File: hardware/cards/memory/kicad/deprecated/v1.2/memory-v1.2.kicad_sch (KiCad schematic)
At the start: 0 parts

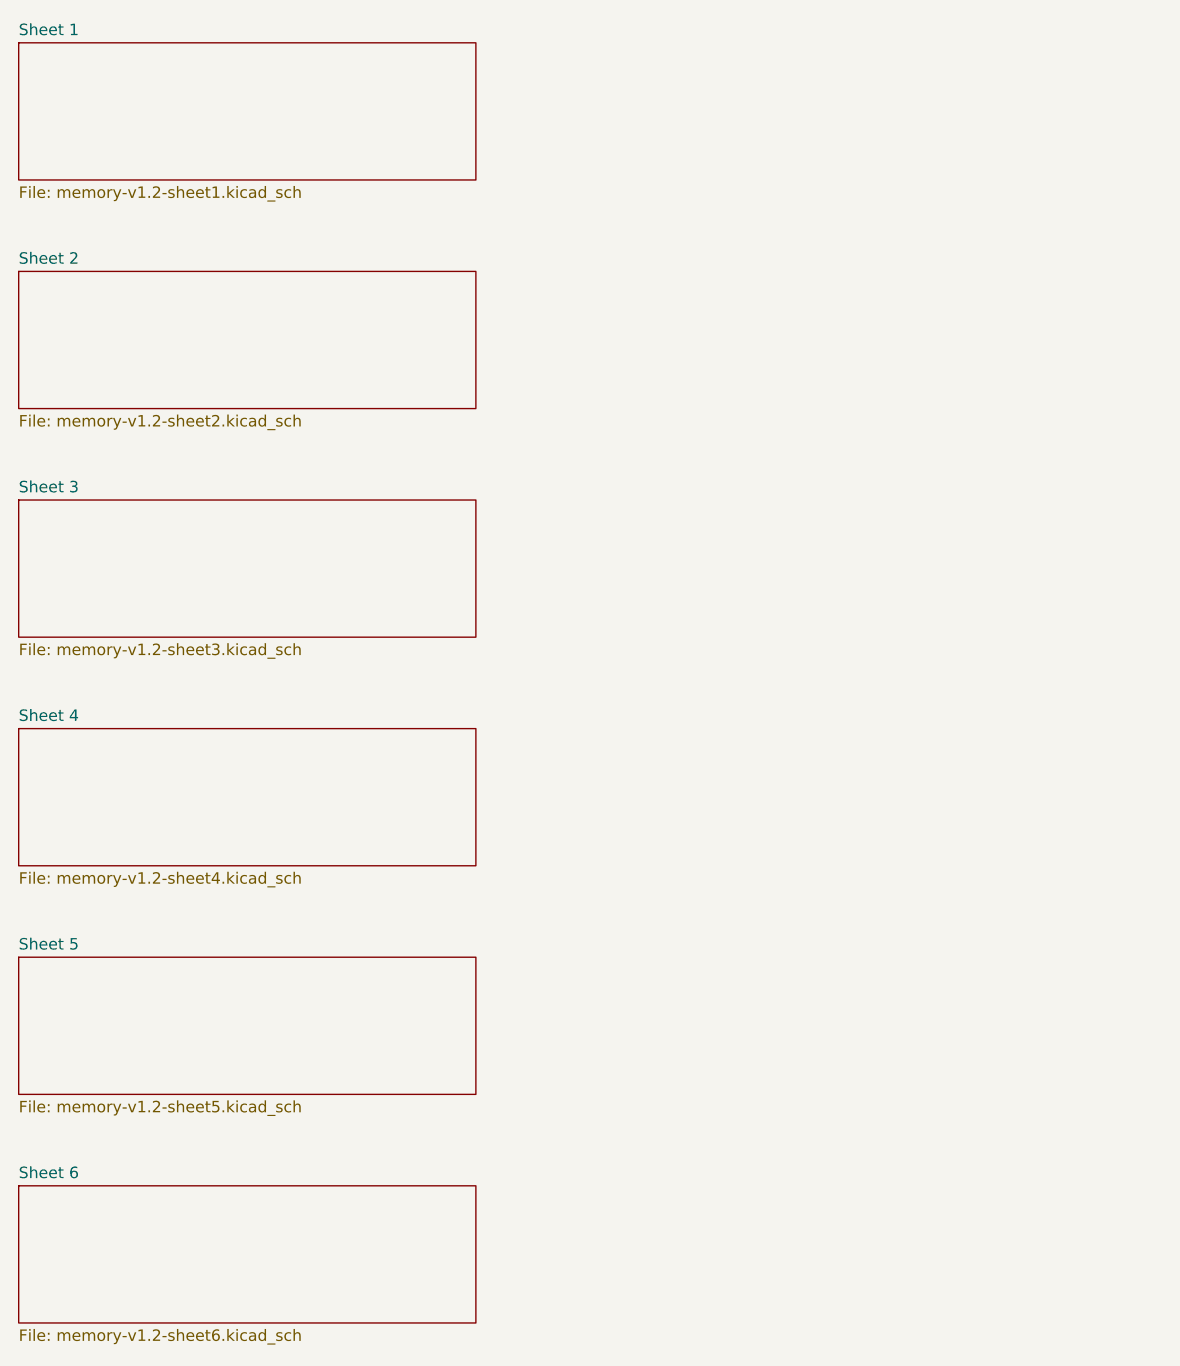
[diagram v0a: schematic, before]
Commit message: fix(kicad): readable converted schematics - overlaps 42,847 -> 3,147, nothing off the frame; CF sheet 0 overlaps
- tools/kicad/sch_overlaps.py: calibrated readability check (text/text, text/body, text/line, off frame/title block)
- eagle_sch_to_kicad.py: fields placed from Eagle's smashed attributes or the symbol's >NAME/>VALUE with Eagle's align,
  size and ratio, readable angles; fields Eagle never shows hidden (FABC96R shows only its pin name); pin numbers hidden
  where every Eagle pin hides them; Eagle-hidden layers dropped (the stray SpiceOrder text); labels on their own wires,
  converter labels only where KiCad needs them; rotate-then-mirror fixed for MR90/MR270 in pin_world/no-connects;
  each sheet on the smallest page that holds it, centred clear of the title block
- finish_board.py: stable footprint-library choice (DRC counts no longer vary run to run)
- all 37 projects regenerated: netlist proofs unchanged (34 MATCH, 2 schematic-only, video Fusion export MISMATCH as
  before); DRC same or better; ERC up (loose wire ends onto graphic buses no longer hidden by labels; explained per README)
- CF card: gate names off the gate bodies, U3 clear of its title, 5.08 mm connector pins; rebuilt: DRC 0/0, proof MATCH
- schematic PDFs regenerated (tools/sch_to_pdf.py, 37/37)

Co-Authored-By: Claude Opus 5.5 <noreply@anthropic.com>
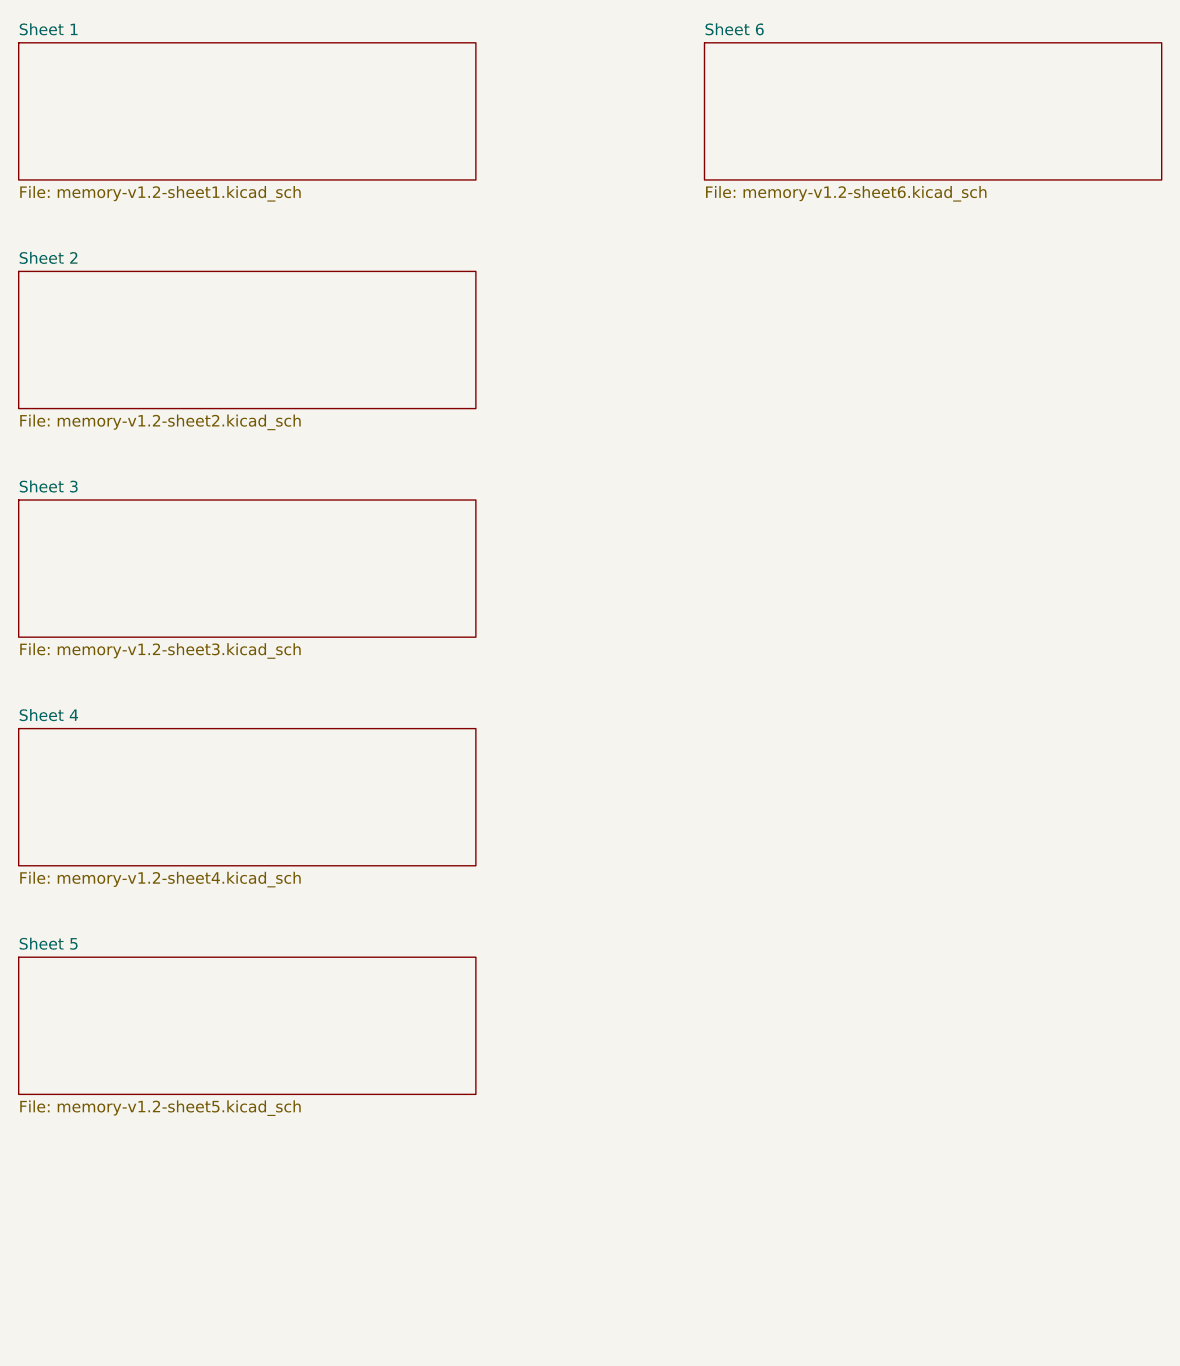
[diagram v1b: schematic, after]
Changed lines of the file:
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@@
 		(instances (project "memory-v1.2" (path "/af66b66e-c3aa-f1a5-6d3e-e2820af0deba" (page "6"))))
 	)
-	(sheet (at 25.4 152.4) (size 50.8 15.24) (exclude_from_sim no) (in_bom yes) (on_board yes) (dnp no) (fields_autoplaced yes)
+	(sheet (at 101.6 25.4) (size 50.8 15.24) (exclude_from_sim no) (in_bom yes) (on_board yes) (dnp no) (fields_autoplaced yes)
 		(stroke (width 0.1524) (type solid)) (fill (color 0 0 0 0.0))
-		(property "Sheetname" "Sheet 6" (at 25.4 151.7 0) (effects (font (size 1.27 1.27)) (justify left bottom)))
-		(property "Sheetfile" "memory-v1.2-sheet6.kicad_sch" (at 25.4 168.3 0) (effects (font (size 1.27 1.27)) (justify left top)))
+		(property "Sheetname" "Sheet 6" (at 101.6 24.7 0) (effects (font (size 1.27 1.27)) (justify left bottom)))
+		(property "Sheetfile" "memory-v1.2-sheet6.kicad_sch" (at 101.6 41.3 0) (effects (font (size 1.27 1.27)) (justify left top)))
 		(instances (project "memory-v1.2" (path "/af66b66e-c3aa-f1a5-6d3e-e2820af0deba" (page "7"))))
 	)
